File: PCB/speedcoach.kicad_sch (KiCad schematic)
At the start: 0 parts

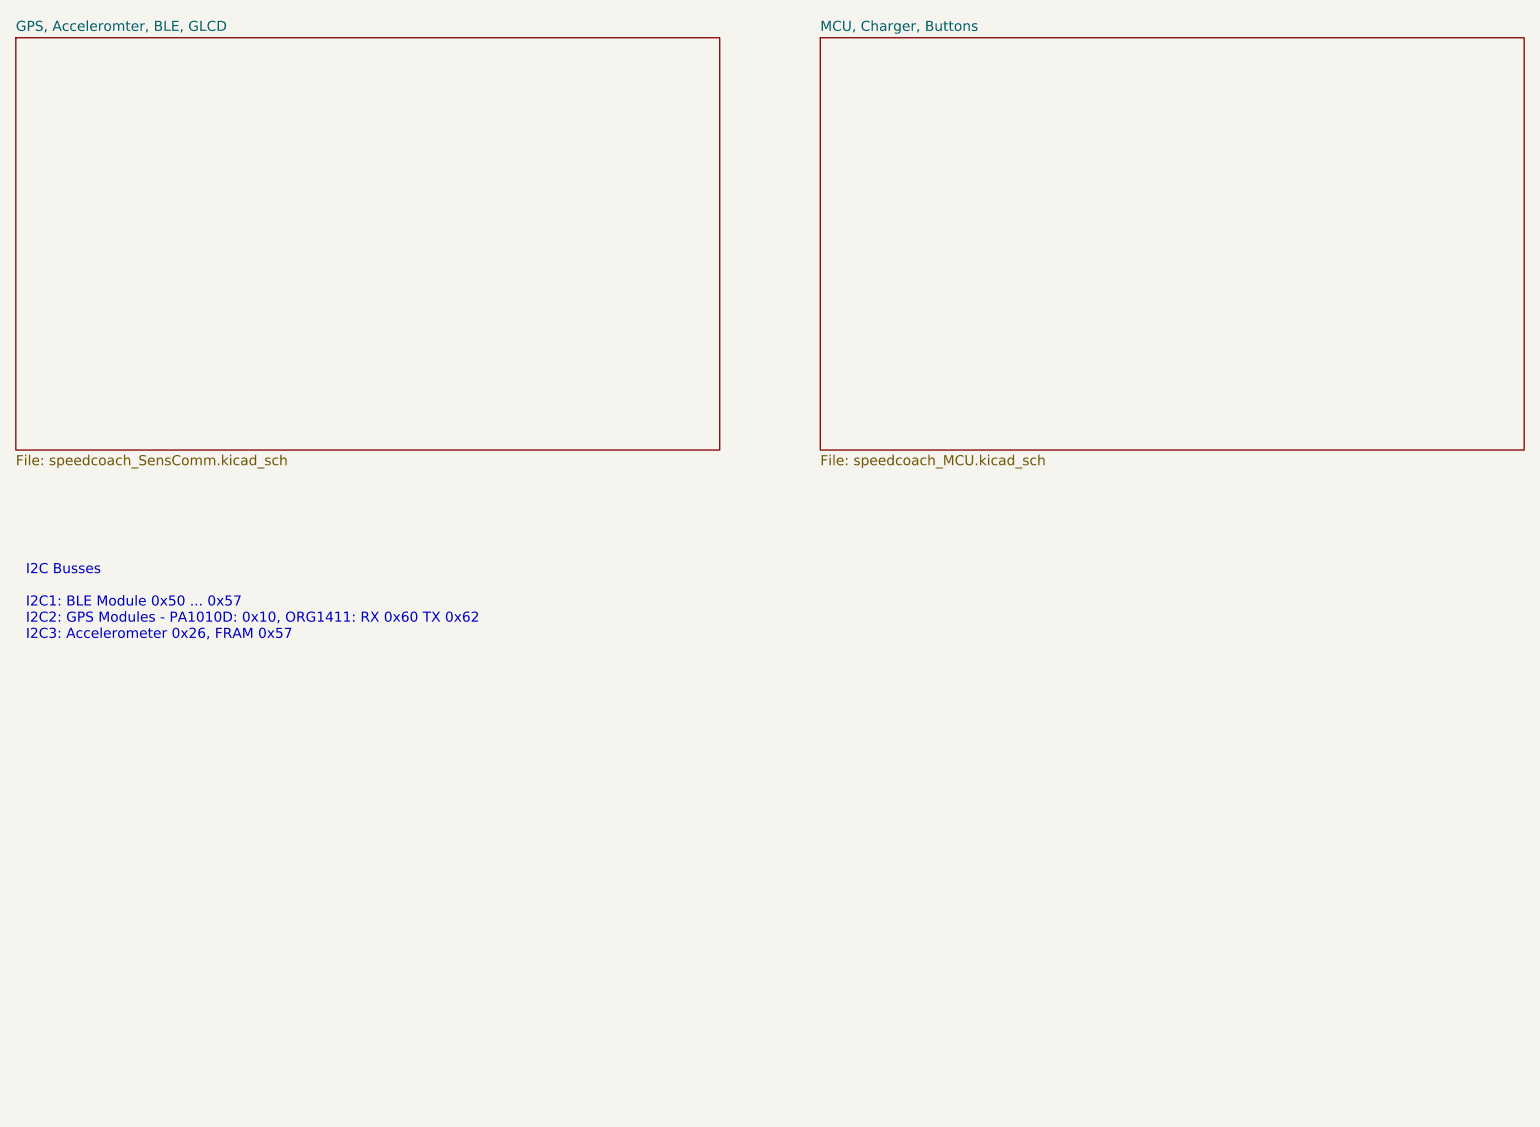
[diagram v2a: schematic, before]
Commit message: updated some labels, finetuning
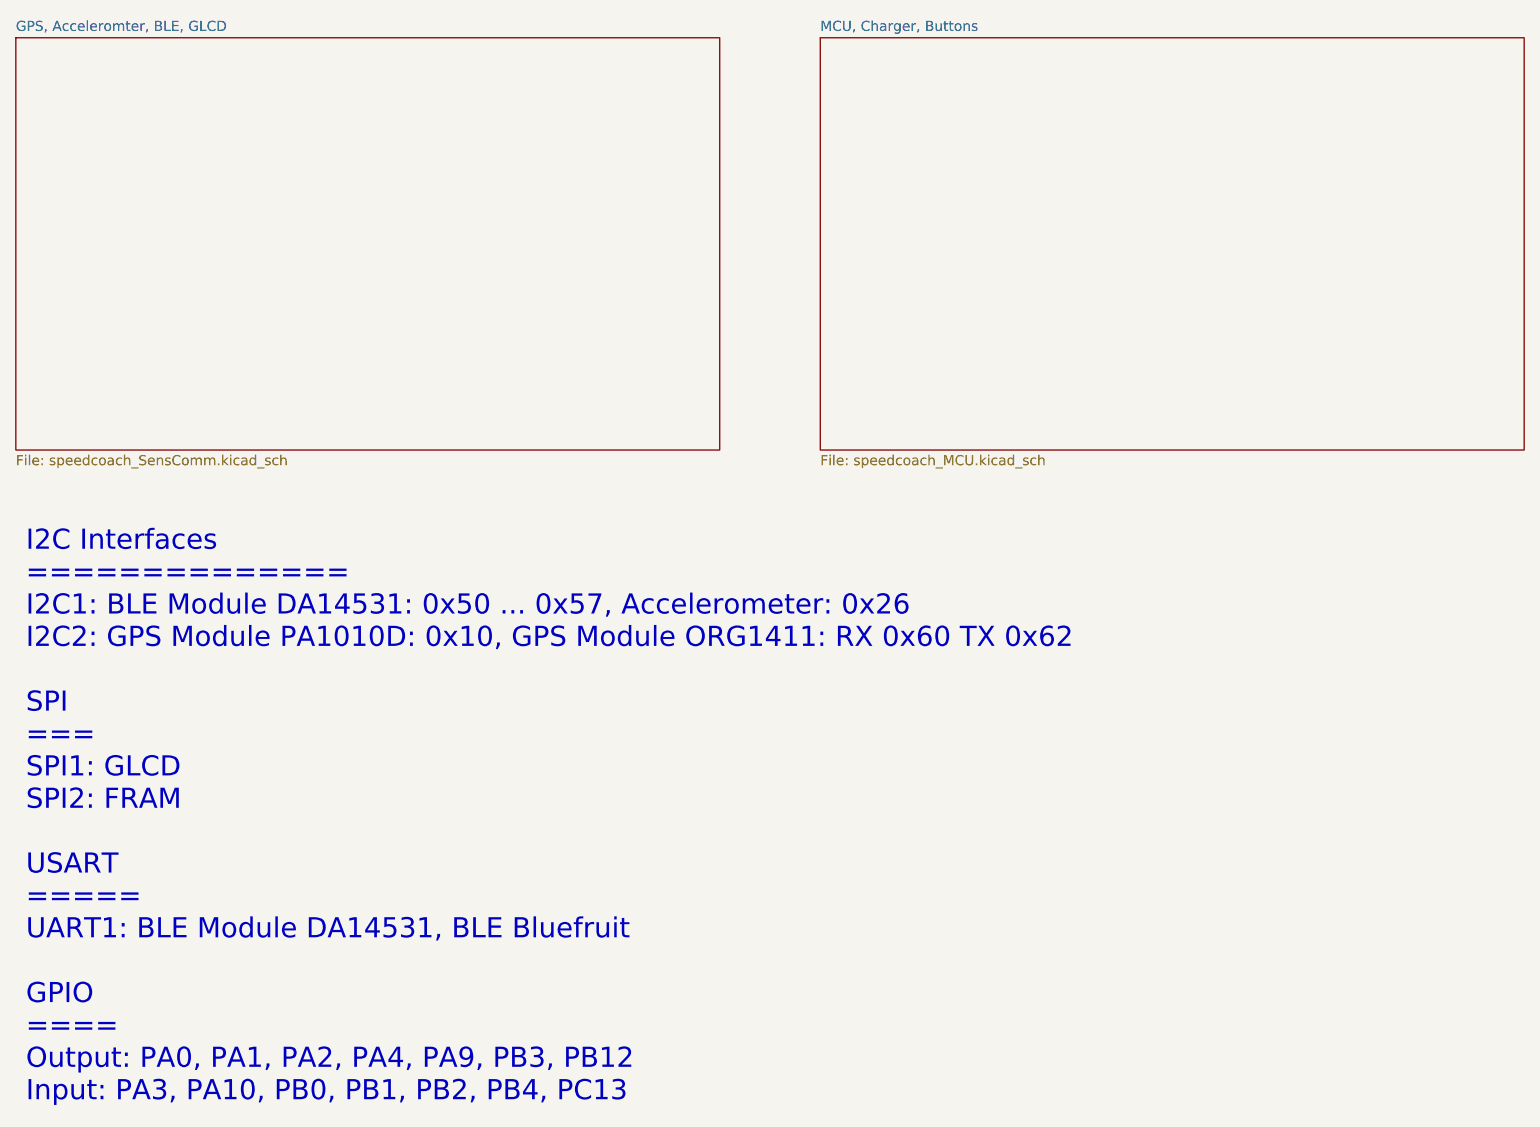
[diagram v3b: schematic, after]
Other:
- note added: "I2C Interfaces ============== I2C1: BLE Module DA14531: 0x50 ... 0x57, Accelerometer: 0x26 I2C2: GPS Module PA1010D: 0x10, GPS Module ORG1411: RX 0x60 TX 0x62 SPI === SPI1: GLCD SPI2: FRAM USART ===== UART1: BLE Module DA14531, BLE Bluefruit GPIO ==== Output: PA0, PA1, PA2, PA4, PA9, PB3, PB12 Input: PA3, PA10, PB0, PB1, PB2, PB4, PC13"
- note removed: "I2C Busses I2C1: BLE Module 0x50 ... 0x57 I2C2: GPS Modules - PA1010D: 0x10, ORG1411: RX 0x60 TX 0x62 I2C3: Accelerometer 0x26, FRAM 0x57"
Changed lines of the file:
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@@
     (company "Peter Horauer")
   )
-  (text "I2C Busses\n\nI2C1: BLE Module 0x50 ... 0x57\nI2C2: GPS Modules - PA1010D: 0x10, ORG1411: RX 0x60 TX 0x62\nI2C3: Accelerometer 0x26, FRAM 0x57"
-    (at 39.37 114.3 0)
-    (effects (font (size 1.27 1.27)) (justify left bottom))
+  (text "I2C Interfaces\n==============\nI2C1: BLE Module DA14531: 0x50 ... 0x57, Accelerometer: 0x26\nI2C2: GPS Module PA1010D: 0x10, GPS Module ORG1411: RX 0x60 TX 0x62\n\nSPI\n===\nSPI1: GLCD\nSPI2: FRAM\n\nUSART\n=====\nUART1: BLE Module DA14531, BLE Bluefruit\n\nGPIO\n====\nOutput: PA0, PA1, PA2, PA4, PA9, PB3, PB12\nInput: PA3, PA10, PB0, PB1, PB2, PB4, PC13 "
+    (at 39.37 172.72 0)
+    (effects (font (face "DejaVu Sans Mono") (size 2.54 2.54)) (justify left bottom))
   )
   (sheet (at 38.1 38.1) (size 88.9 52.07) (fields_autoplaced)
@@
       (reference "U8") (unit 1) (value "MCP73831") (footprint "speedcoach:MCP73831T-2ATIOT")
     )
-    (path "/00000000-0000-0000-0000-000062045098/f3bde24f-d653-4e0d-9619-c9d50aba7096"
+    (path "/00000000-0000-0000-0000-000062045098/78b5f2db-9516-41f0-a6e0-99e4c52e2bb6"
       (reference "U9") (unit 1) (value "STM32L051C8T3") (footprint "")
     )
